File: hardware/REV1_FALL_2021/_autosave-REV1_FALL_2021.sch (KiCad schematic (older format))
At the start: 23 parts, among them J101 Screw_Terminal_01x02, Q101 Q_NMOS_GDS, U1 Teensy3.6_All_Pins, U2 PA16165_Breakout, U3 MPL3115A2_Breakout, U4 BNO055_Breakout, U5 RFM69HCW_Breakout

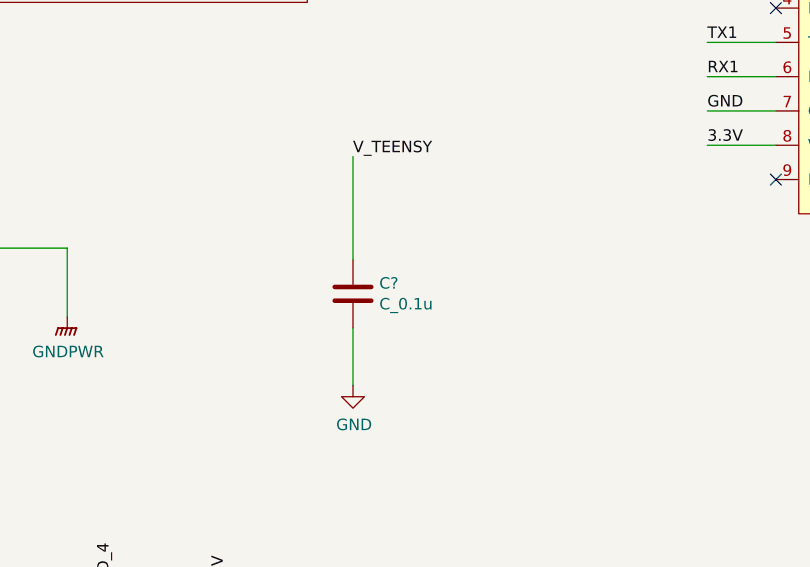
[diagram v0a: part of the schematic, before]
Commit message: add decoupling capacitor on Teensy VIN pin
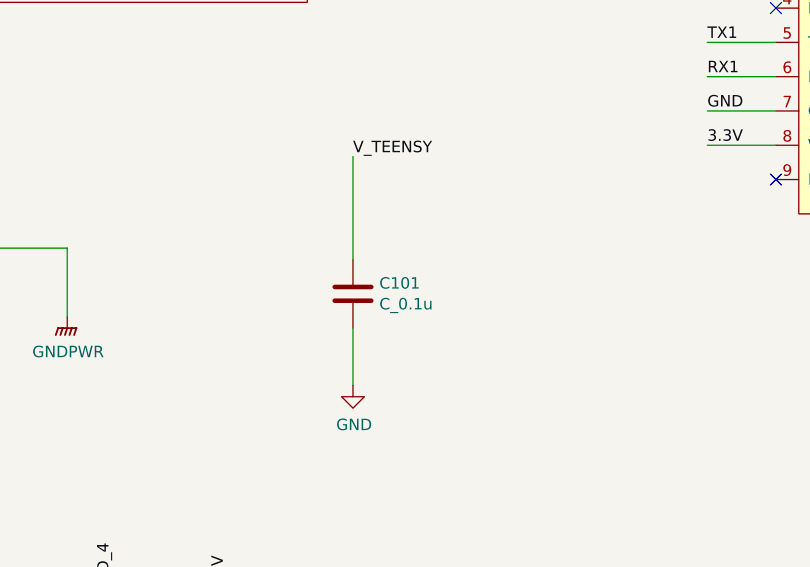
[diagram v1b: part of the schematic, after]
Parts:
- gave numbers to parts that had none: 1
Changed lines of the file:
@@
 3.3V
 $Comp
-L Device:C C?
+L Device:C C101
 U 1 1 61A04C38
 P 3750 7100
-F 0 "C?" H 3865 7146 50  0000 L CNN
+F 0 "C101" H 3865 7146 50  0000 L CNN
 F 1 "C_0.1u" H 3865 7055 50  0000 L CNN
 F 2 "Capacitor_SMD:C_0805_2012Metric_Pad1.18x1.45mm_HandSolder" H 3788 6950 50  0001 C CNN
@@
 $EndComp
 $Comp
-L power:GND #PWR?
+L power:GND #PWR0107
 U 1 1 61A05A03
 P 3750 7500
-F 0 "#PWR?" H 3750 7250 50  0001 C CNN
+F 0 "#PWR0107" H 3750 7250 50  0001 C CNN
 F 1 "GND" H 3755 7327 50  0000 C CNN
 F 2 "" H 3750 7500 50  0001 C CNN
